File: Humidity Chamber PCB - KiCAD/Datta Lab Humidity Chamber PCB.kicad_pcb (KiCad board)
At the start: 2 copper layers, 157.5 x 116.8 mm, 51 parts, among them J1 BNC-1, J10 MFC 3, J11 I2C_STANDARDQWIIC, J12 I2C_STANDARDQWIIC, J13 MFC 2, J14 MFC 4, J15 MFM 1, J16 MFM 2, J17 MFC 1, J18 MFC 3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

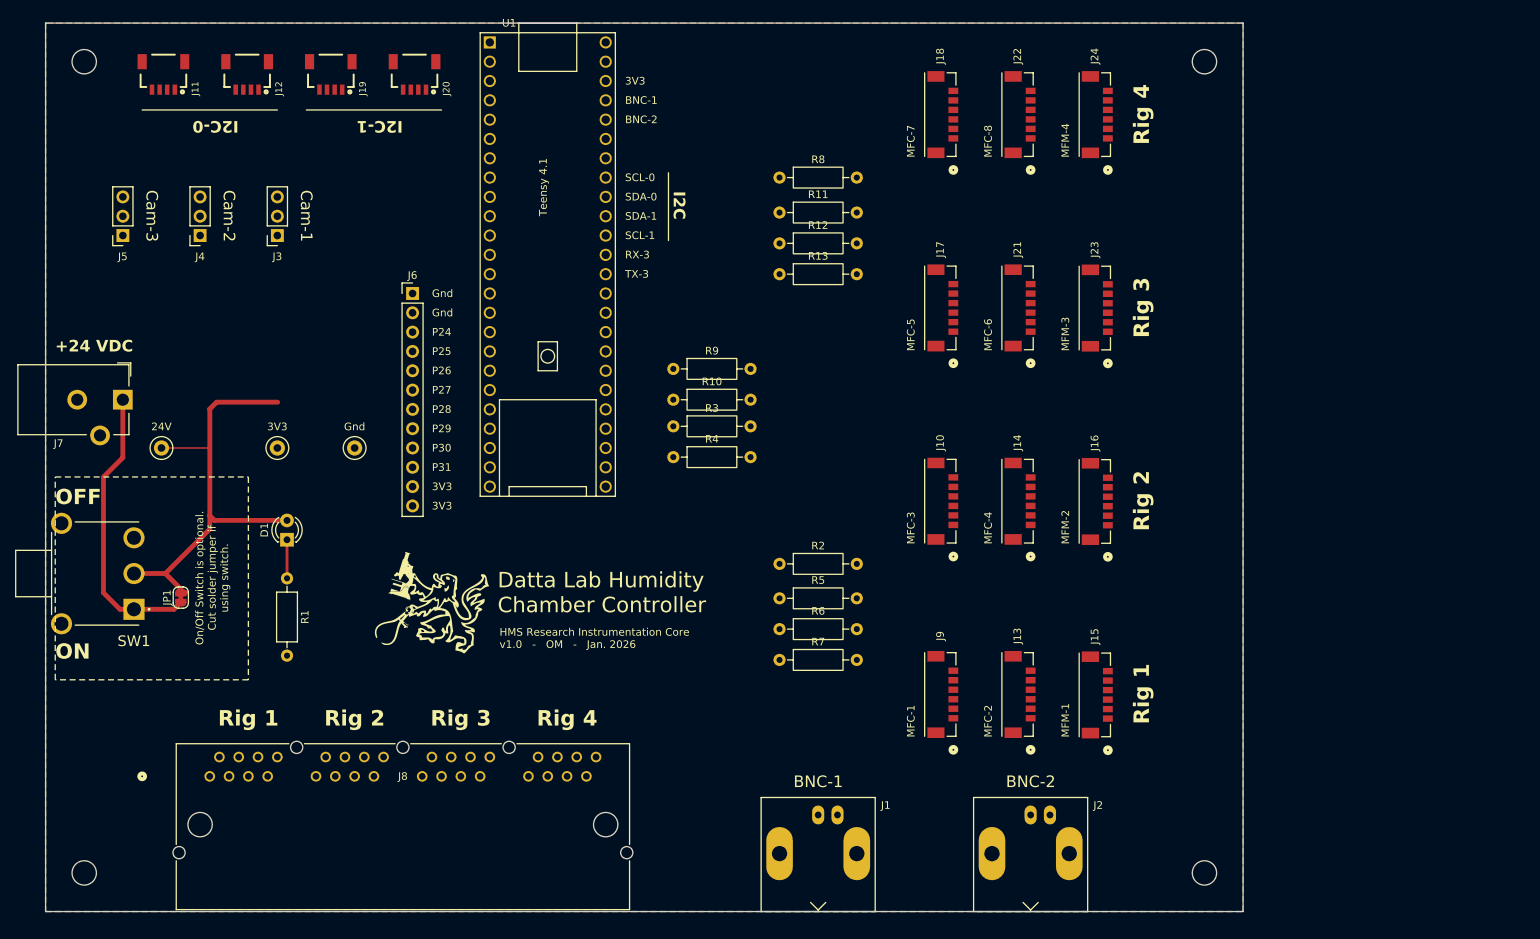
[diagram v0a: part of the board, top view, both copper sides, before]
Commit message: Rearrange board layout per Brian's feedback
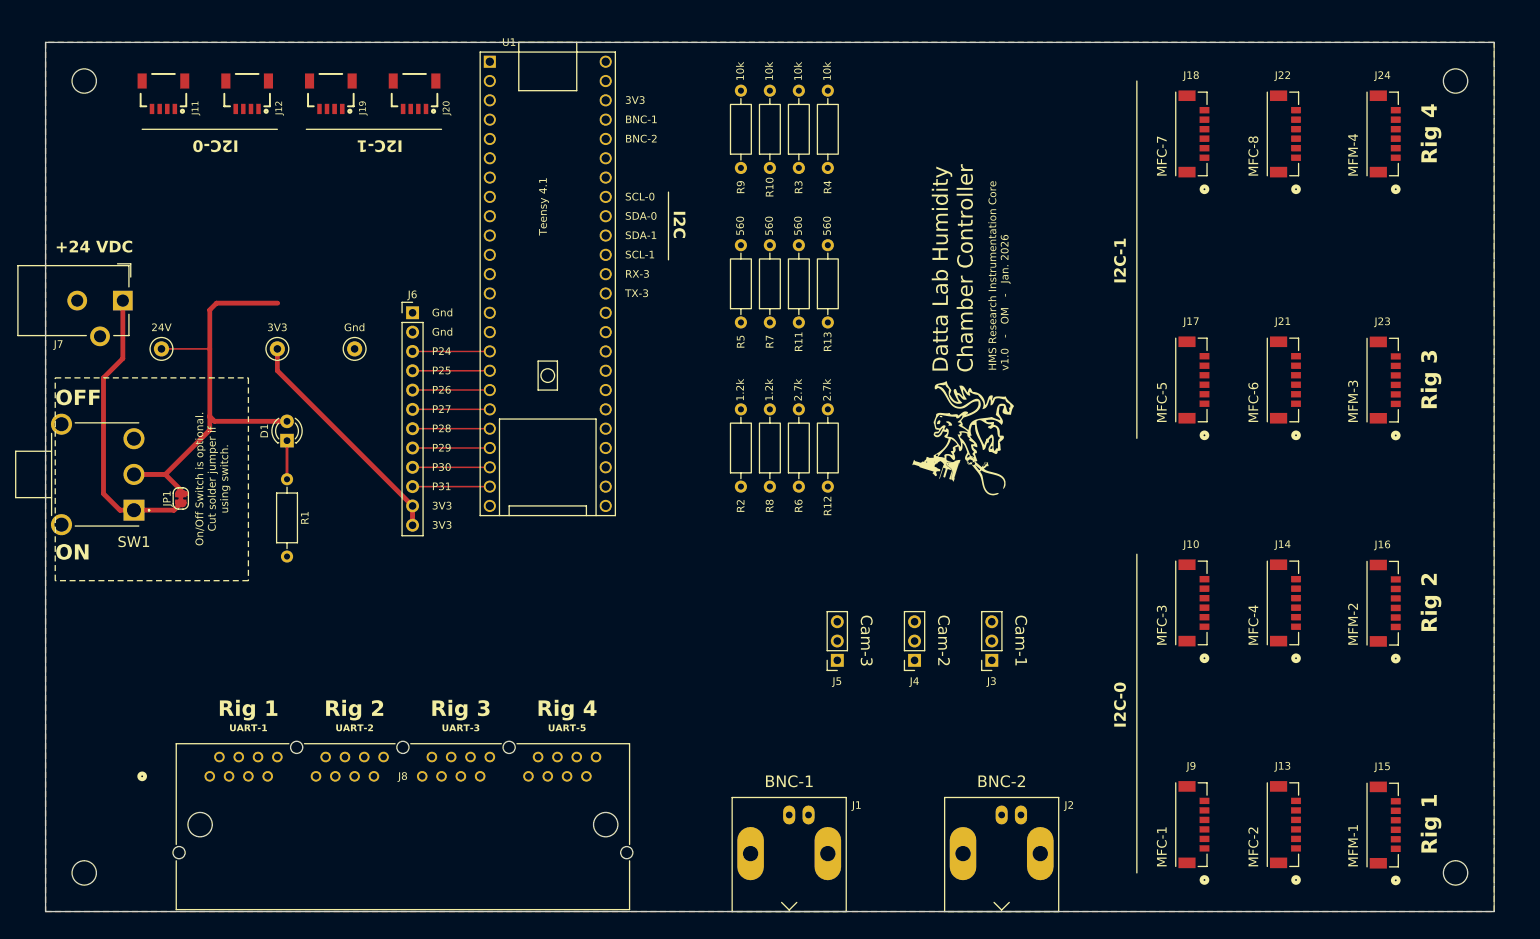
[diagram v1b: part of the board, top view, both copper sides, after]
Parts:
- moved J3 109.3 mm to (147.3, 106.7)
- moved J4 109.3 mm to (137.1, 106.7)
- moved J5 109.3 mm to (127.0, 106.7)
- moved G1 73.1 mm to (143.5, 77.5), turned to 90 degrees
- moved R7 44.4 mm to (118.1, 62.2), turned to 90 degrees
- moved R4 43.1 mm to (125.7, 41.9), turned to 90 degrees
- moved J15 41.5 mm to (198.7, 128.3)
- moved R8 40.7 mm to (118.1, 83.8), turned to 90 degrees
- moved J16 40.2 mm to (198.7, 99.2)
- moved J23 39.0 mm to (198.7, 69.8)
- moved J13 38.9 mm to (185.6, 128.3)
- moved J24 37.9 mm to (198.7, 37.4)
- moved R3 37.8 mm to (121.9, 41.9), turned to 90 degrees
- moved J14 37.4 mm to (185.6, 99.1)
- moved J9 37.2 mm to (173.5, 128.3)
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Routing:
- net +3.3V: track 0.00 -> 30.6 mm
- net Net-(J6-Pin_9): track 0.00 -> 10.2 mm
- net Net-(J6-Pin_8): track 0.00 -> 10.2 mm
- net Net-(J6-Pin_7): track 0.00 -> 10.2 mm
- net Net-(J6-Pin_6): track 0.00 -> 10.2 mm
- net Net-(J6-Pin_5): track 0.00 -> 10.2 mm
- net Net-(J6-Pin_4): track 0.00 -> 10.2 mm
- net Net-(J6-Pin_3): track 0.00 -> 10.2 mm
- net Net-(J6-Pin_10): track 0.00 -> 10.2 mm
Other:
- board size 157.5 x 116.8 mm -> 190.5 x 114.3 mm
- board text added: "UART-1"
- board text added: "UART-2"
- board text added: "UART-3"
- board text added: "UART-5"

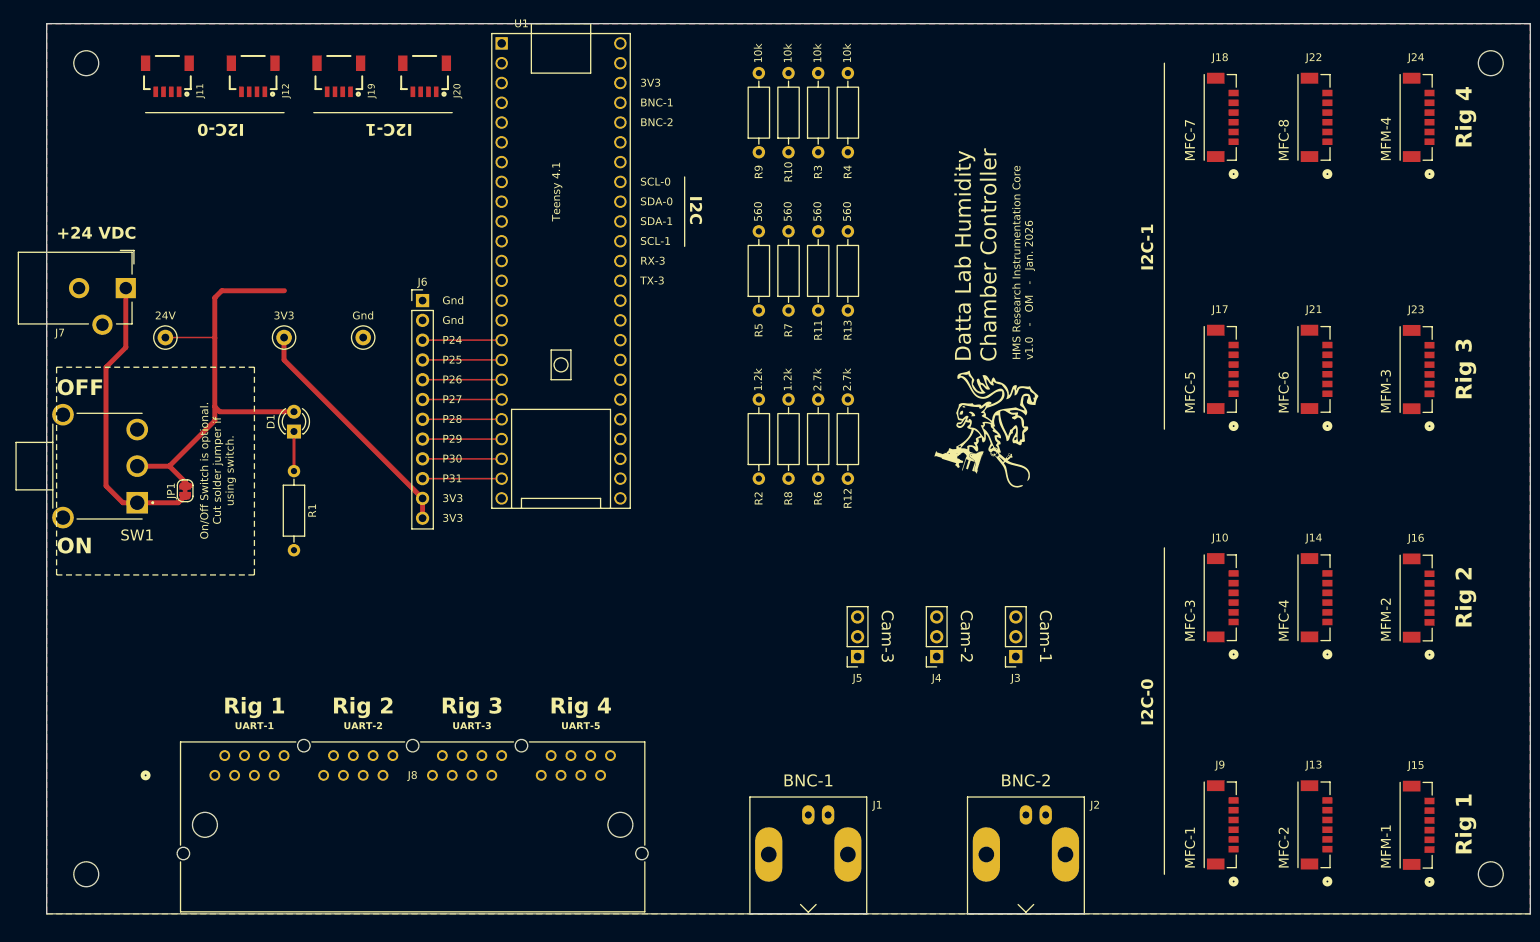
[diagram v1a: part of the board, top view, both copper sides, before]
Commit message: Routed all traces
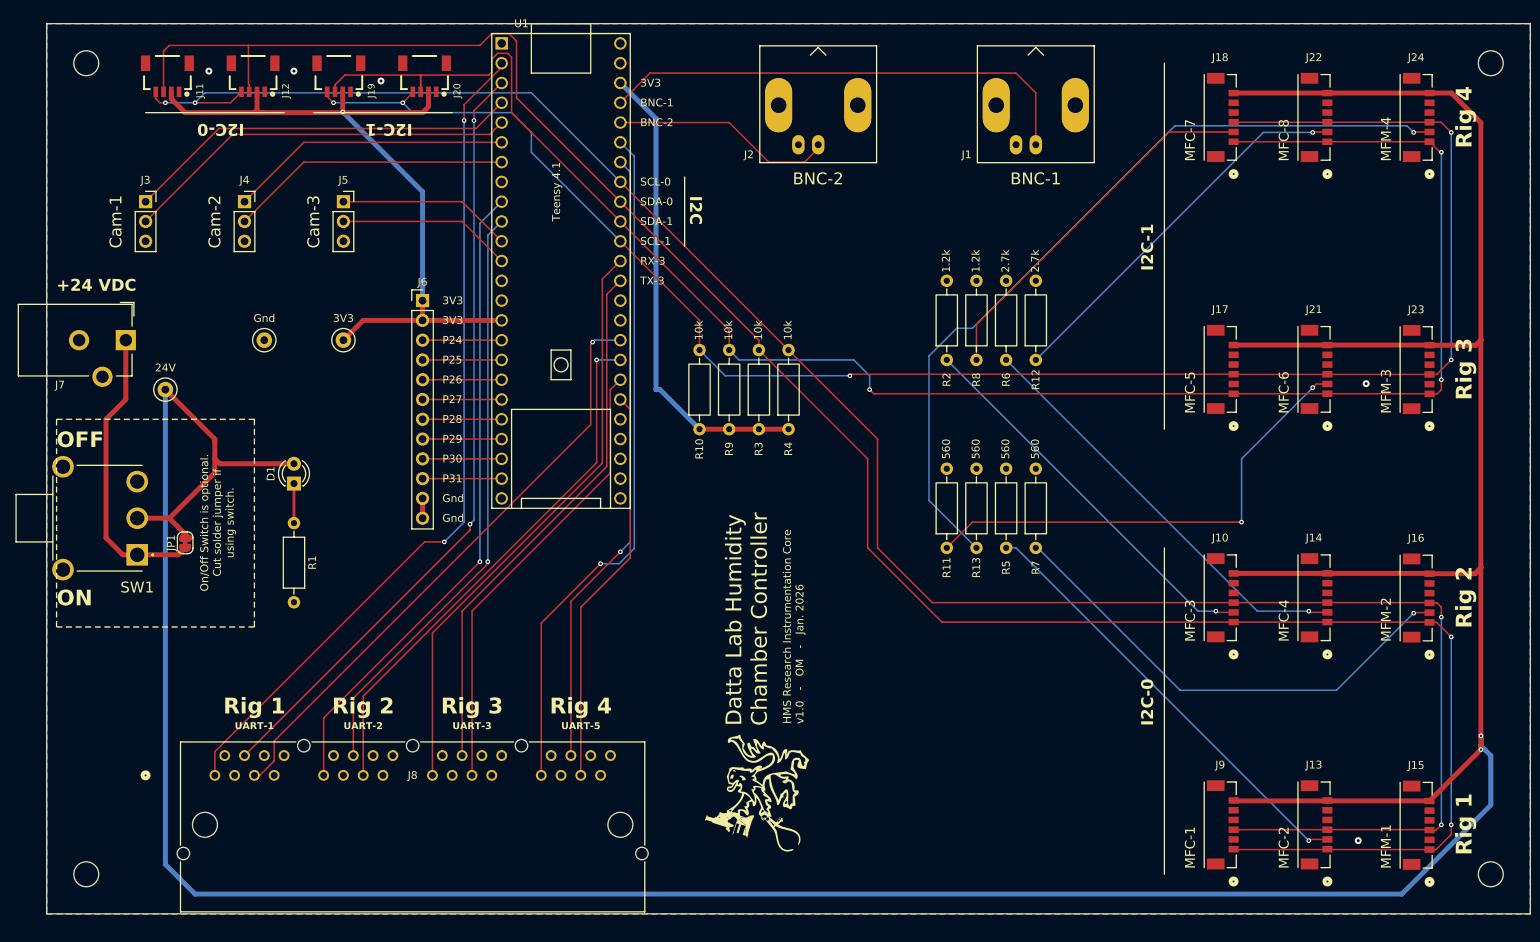
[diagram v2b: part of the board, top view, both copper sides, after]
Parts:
- moved J3 126.1 mm to (35.6, 48.3), turned to 0 degrees
- moved J4 106.3 mm to (48.3, 48.3), turned to 0 degrees
- moved J1 90.9 mm to (149.9, 41.0), turned to 0 degrees
- moved J2 90.1 mm to (121.9, 41.0), turned to 0 degrees
- moved J5 88.1 mm to (61.0, 48.3), turned to 0 degrees
- moved G1 55.2 mm to (114.0, 124.2)
- moved R5 44.0 mm to (146.1, 92.7)
- moved R7 44.0 mm to (149.9, 92.7)
- moved R10 37.4 mm to (106.7, 77.5)
- moved R3 36.4 mm to (114.3, 77.5)
- moved R4 36.4 mm to (118.1, 77.5)
- moved R9 35.8 mm to (110.5, 77.5)
- moved R11 34.7 mm to (138.4, 92.7)
- moved R13 34.7 mm to (142.2, 92.7)
- moved R12 28.5 mm to (149.9, 68.6)
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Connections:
- J6 pad 1: GND -> +3.3V
- J6 pad 11: +3.3V -> GND
- J6 pad 12: +3.3V -> GND
- J6 pad 2: GND -> +3.3V
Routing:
- net +24V: track 58.4 -> 500.0 mm, vias 0 -> 2
- net /SDA-0: track 0.00 -> 275.4 mm, vias 0 -> 2
- net /SCL-0: track 0.00 -> 263.7 mm, vias 0 -> 4
- net /SDA-1: track 0.00 -> 230.5 mm, vias 0 -> 3
- net /SCL-1: track 0.00 -> 224.0 mm, vias 0 -> 5
- net +3.3V: track 30.6 -> 156.4 mm, vias 0 -> 1
- net /RX-1: track 0.00 -> 108.2 mm, vias 0 -> 2
- net Net-(J24-Pin_2): track 0.00 -> 104.1 mm, vias 0 -> 1
- net /TX-1: track 0.00 -> 100.0 mm, vias 0 -> 2
- net /RX-5: track 0.00 -> 88.4 mm, vias 0 -> 1
- net /RX-2: track 0.00 -> 83.1 mm, vias 0 -> 1
- net /TX-5: track 0.00 -> 79.9 mm, vias 0 -> 1
- net /GPIO-1: track 0.00 -> 77.7 mm, vias 0 -> 1
- net /TX-2: track 0.00 -> 76.5 mm, vias 0 -> 1
- net /RX-3: track 0.00 -> 76.0 mm
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
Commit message: Minor cosmetic adjustments
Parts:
- removed H3, H4: MountingHole, MountingHole:MountingHole_3.2mm_M3
- moved TP2 49.1 mm to (55.9, 118.1)
- moved J11 16.3 mm to (51.1, 44.3)
- moved J12 16.3 mm to (62.1, 44.3)
- moved J20 16.3 mm to (84.1, 44.3)
- moved J4 16.3 mm to (61.0, 58.4)
- moved J8 16.3 mm to (57.1, 132.1)
- moved D1 16.3 mm to (67.3, 94.6)
- moved H1 16.3 mm to (40.6, 40.6)
- moved J19 16.3 mm to (73.1, 44.3)
- moved J2 16.3 mm to (134.6, 51.1)
- moved J3 16.3 mm to (48.3, 58.4)
- moved J5 16.3 mm to (73.7, 58.4)
- moved JP1 16.3 mm to (53.3, 102.2)
- moved R1 16.3 mm to (67.3, 99.7)
- moved R3 16.3 mm to (127.0, 87.6)
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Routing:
- net +3.3V: track 156.4 -> 192.9 mm, vias 1 -> 2
- net +24V: track 500.0 -> 471.2 mm
- net /SDA-0: track 275.4 -> 278.7 mm
- net /SDA-1: track 230.5 -> 233.2 mm
- net /SCL-1: track 224.0 -> 225.9 mm
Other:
- board text added: "C3-1"
- board text added: "C3-2"
- board text added: "Cam1-1"
- board text added: "Cam1-2"
- board text added: "Cam2-1"
- board text added: "Cam2-2"
- board text added: "GPIO-1"
- board text added: "GPIO-2"
- board text added: "GPIO-3"
- board text added: "GPIO-5"
- board text added: "RX-1"
- board text added: "RX-2"
- board text added: "RX-5"
- board text added: "TX-1"
- board text added: "TX-2"
- board text added: "TX-5"

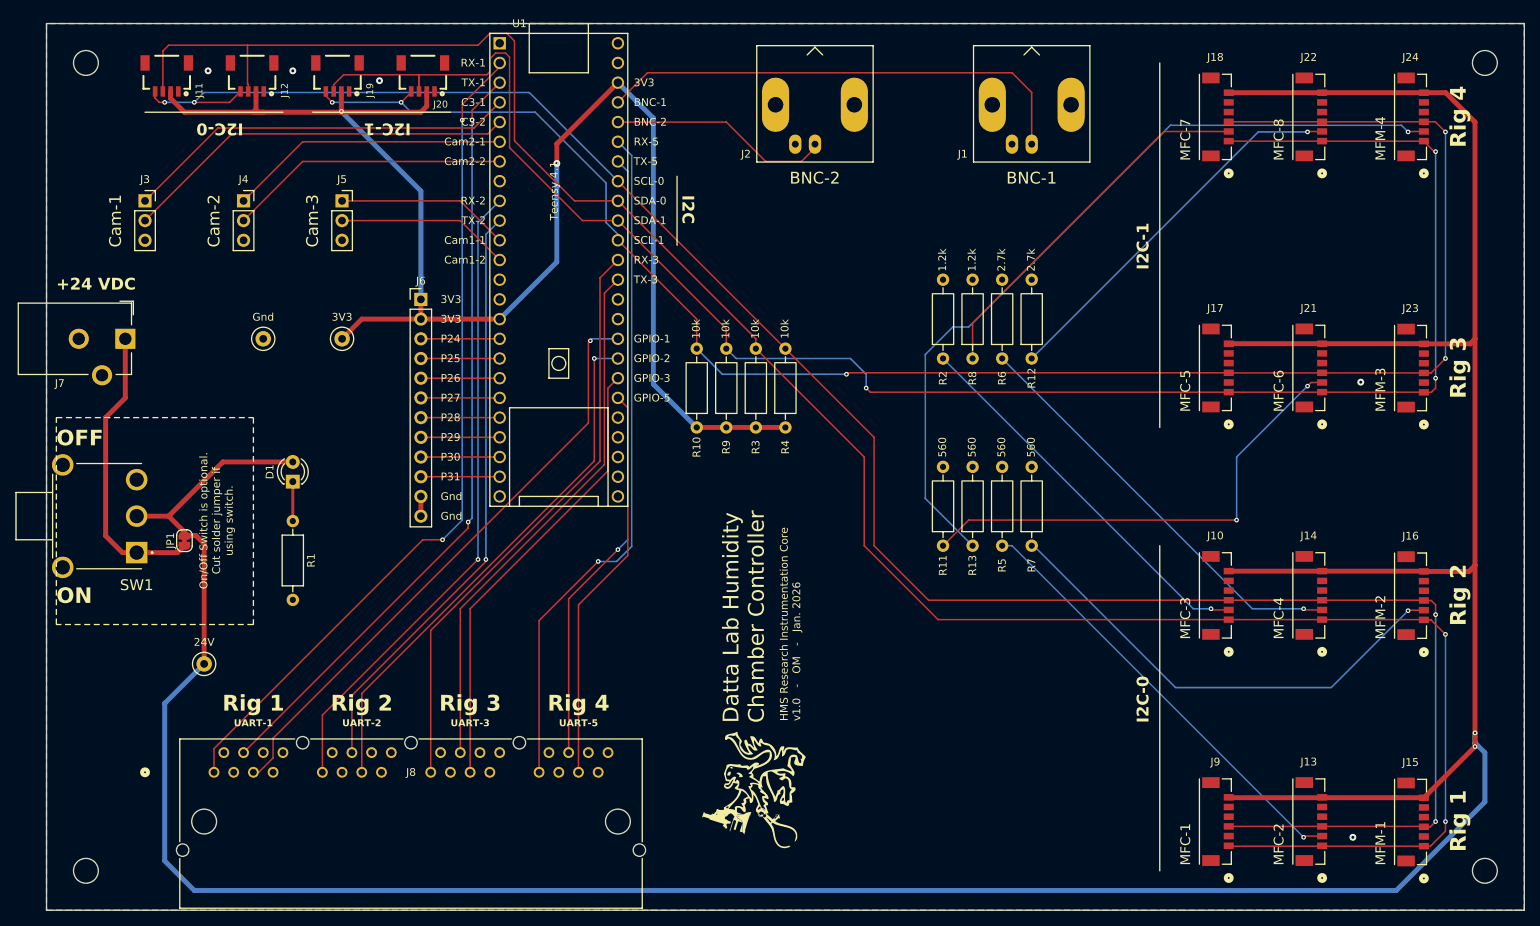
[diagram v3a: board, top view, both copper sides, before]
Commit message: Rounded PCB corners; More minor fixes
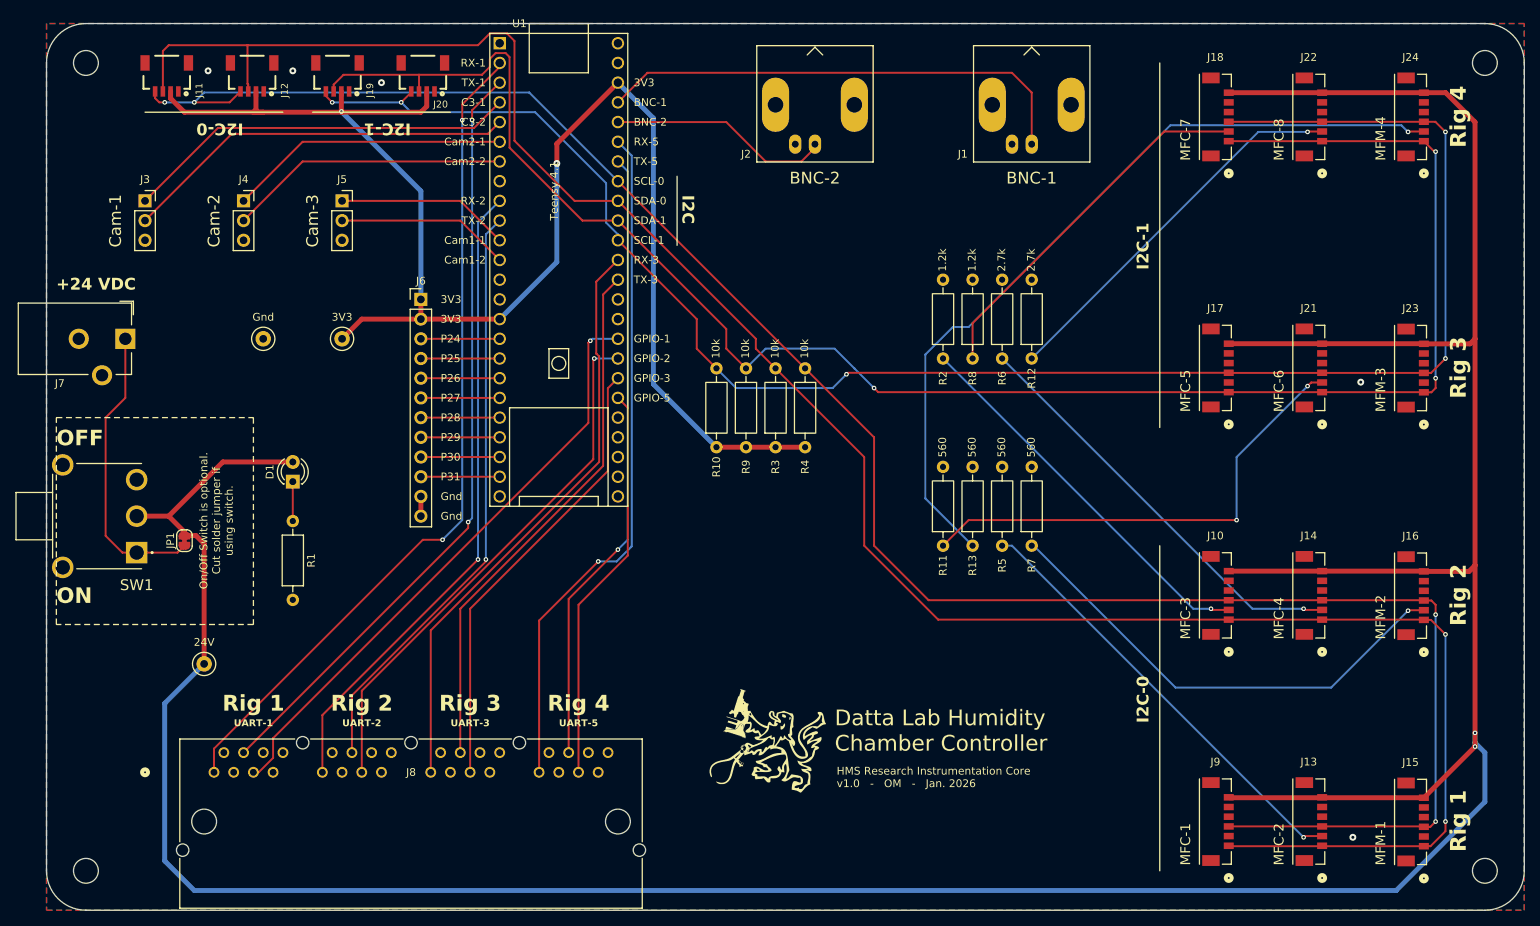
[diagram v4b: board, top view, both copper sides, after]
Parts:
- moved G1 6.59 mm to (128.5, 128.0), turned to 0 degrees
- moved R10 3.59 mm to (121.9, 90.2)
- moved R9 3.59 mm to (125.7, 90.2)
- moved R3 3.59 mm to (129.5, 90.2)
- moved R4 3.59 mm to (133.3, 90.2)
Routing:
- net +3.3V: track 192.9 -> 196.5 mm
- net /SCL-1: track 225.9 -> 227.4 mm
- net /SDA-1: track 233.2 -> 233.9 mm
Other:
- outline, holes or cut-outs redrawn
